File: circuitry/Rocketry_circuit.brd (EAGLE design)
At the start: 150 x 33 mm, 7 parts

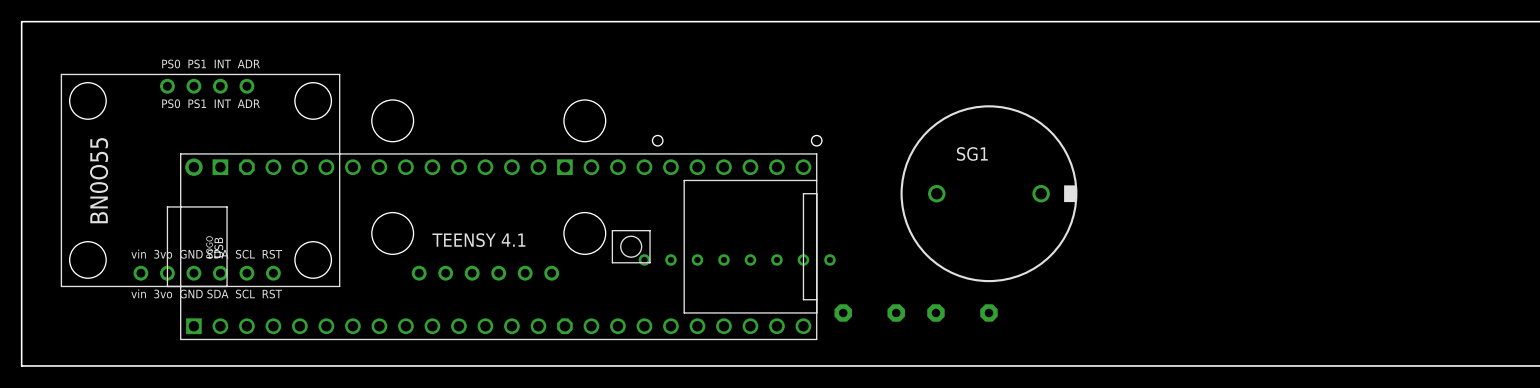
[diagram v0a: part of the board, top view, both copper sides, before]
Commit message: Added 3D files and proper footprints for all components, worked on brd design
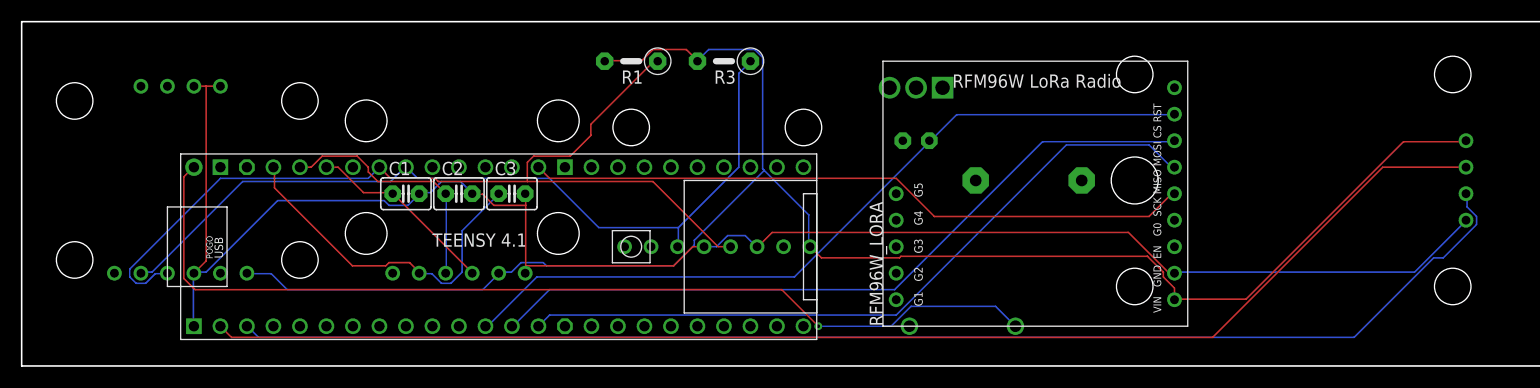
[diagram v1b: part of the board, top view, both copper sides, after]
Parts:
- removed SG1: EFBAA40D101, buzzer:EFBAA40D101
- added C1, C2, C3: 50p, capacitor-wima:C2.5-3
- added C4: 10u, capacitor-wima:C2.5-3
- added D1: 1N4004, diode:DO41-10
- added G1: 3V11R, battery:3V11R
- added IC1: TC1264-3.3VAB, TC1264-3.3VAB:TO254P483X988X2222-3P
- added U$4: NEO6M, NEO6M:NEO6M
- added U$5: RFM96W, RMF96W_lora:RFM96W
- moved R1 33.2 mm to (58.4, 29.2), flipped to the top
- moved R3 33.2 mm to (67.3, 29.2), flipped to the top
- moved BRKOUT1 27.9 mm to (2.54, 7.62), flipped to the bottom
- moved U$2 16.6 mm to (55.9, 8.89)
- moved U$3 2.54 mm to (30.5, 7.62)
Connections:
- new net N$1: C1.1, U$1.21-A7/RX5/BCLK1, U$3.X
- new net N$10: U$1.11-MOSI/CTX1, U$5.MOSI
- new net N$11: U$1.10-CS\MQSR, U$5.CS
- new net N$12: D1.A, G1.+, IC1.1
- new net N$2: C2.1, U$1.22-A8/CTX1, U$3.Y
- new net N$4: C3.1, U$1.23-A9/CRX1/MCLK1, U$3.Z
- new net N$6: U$1.0-RX1/CS1/CRX2, U$4.RX
- new net N$7: U$1.1-TX1/MISO1/CTX2, U$4.TX
- new net N$8: U$1.13-SCK/LED, U$5.SCK
- new net N$9: U$1.12-MISO/MQSL, U$5.MISO
- net +3V3: now also C4.1, IC1.3, U$2.VIN, U$3.3.3V, U$4.VCC, U$5.VIN
- net +5V: now also D1.C
- net GND: now also C1.2, C2.2, C3.2, C4.2, G1.-, IC1.2, U$2.GND, U$2.SDO, U$3.GND, U$4.GND, U$5.GND
- net N$3: now also U$1.19-A5/SCL0, U$2.SCK; no longer U$1.26-A12/MOSI1
- net N$5: now also U$1.18-A4/SDA0, U$2.SDI; no longer U$1.25-A11/RX6/SDA2
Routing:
- net GND: track 0.00 -> 166.8 mm
- net +3V3: track 0.00 -> 164.9 mm
- net N$6: track 0.00 -> 126.6 mm
- net N$7: track 0.00 -> 126.2 mm
- net +5V: track 0.00 -> 94.3 mm, vias 0 -> 1
- net N$3: track 0.00 -> 88.8 mm
- net N$5: track 0.00 -> 78.9 mm
- net N$11: track 0.00 -> 74.5 mm
- net N$10: track 0.00 -> 70.9 mm
- net N$9: track 0.00 -> 69.0 mm
- net N$8: track 0.00 -> 63.9 mm
- net N$4: track 0.00 -> 33.6 mm
- net N$2: track 0.00 -> 23.8 mm
- net N$1: track 0.00 -> 18.2 mm

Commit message: power circuitry up to date
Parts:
- added C5: 100u, capacitor-wima:C2.5-3
- added D2: 1N4004, diode:DO41-10
- moved G1 6.38 mm to (97.2, 24.1)
- moved IC1 6.38 mm to (81.9, 27.3), turned to 180 degrees
- moved D1 1.27 mm to (91.4, 3.81)
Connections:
- net +5V: now also D2.C
- net GND: now also C5.1
- net N$12: now also C5.2, D2.A
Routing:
- net GND: track 166.8 -> 0.00 mm
- net +3V3: track 164.9 -> 0.00 mm
- net N$6: track 126.6 -> 0.00 mm
- net N$7: track 126.2 -> 0.00 mm
- net +5V: track 94.3 -> 0.00 mm, vias 1 -> 0
- net N$3: track 88.8 -> 0.00 mm
- net N$5: track 78.9 -> 0.00 mm
- net N$11: track 74.5 -> 0.00 mm
- net N$10: track 70.9 -> 0.00 mm
- net N$9: track 69.0 -> 0.00 mm
- net N$8: track 63.9 -> 0.00 mm
- net N$4: track 33.6 -> 0.00 mm
- net N$2: track 23.8 -> 0.00 mm
- net N$1: track 18.2 -> 0.00 mm
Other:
- board text added: "Add Decals and names etc"
- board text added: "Add redundancy pads and connections"

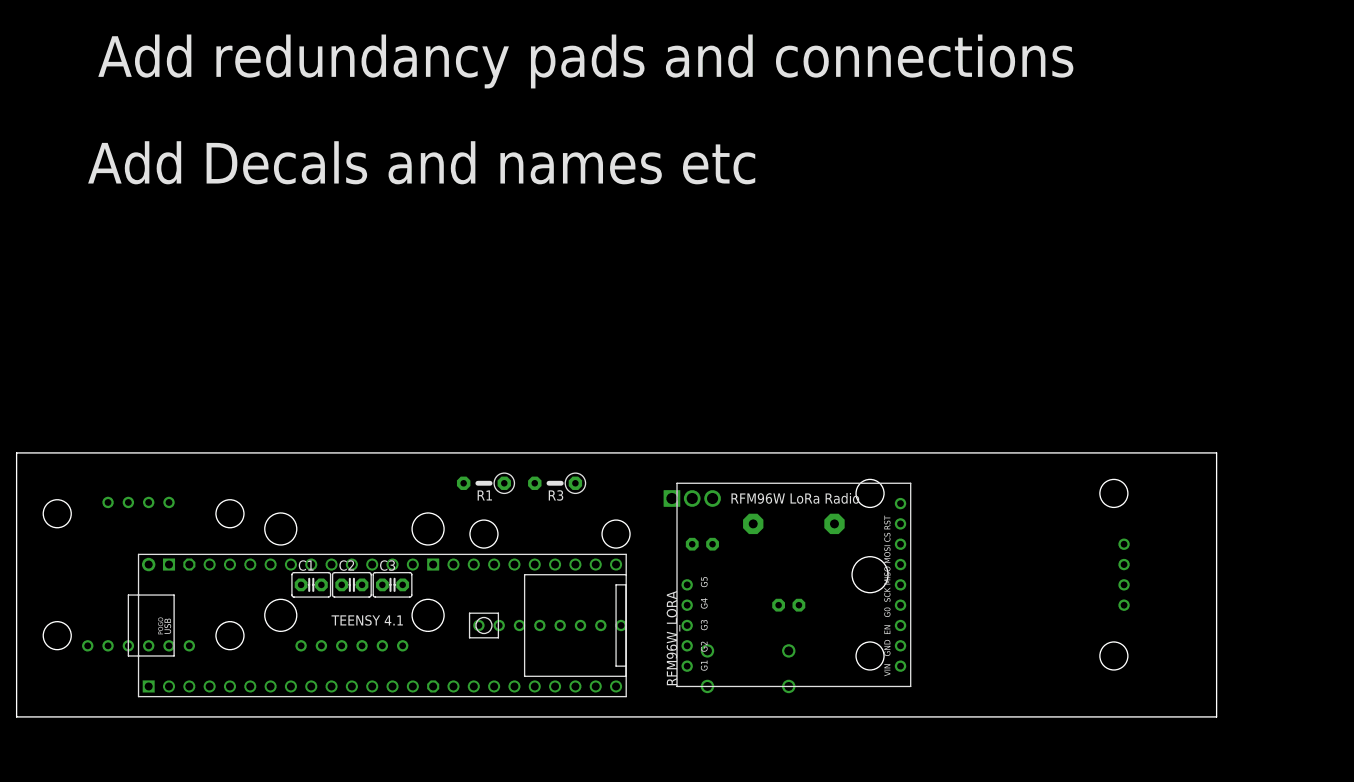
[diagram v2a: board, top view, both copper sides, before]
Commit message: updated board size to 31.75mm width, to fit into 34mm transition shoulder section
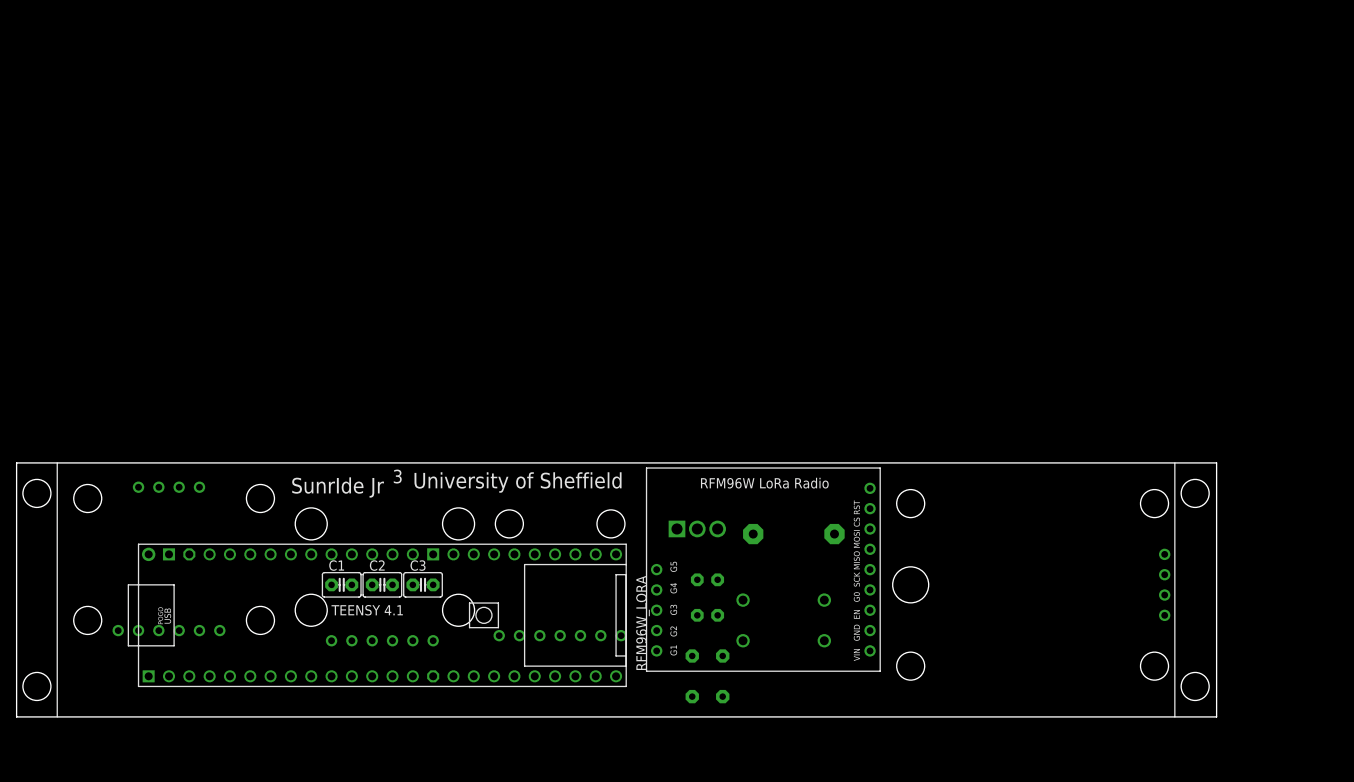
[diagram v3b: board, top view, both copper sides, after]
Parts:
- U$2: value BMP388 -> BMP280; device BMP388:BMP388 -> BMP280:BMP280
- moved R1 35.5 mm to (84.5, 5.08), flipped to the bottom, turned to 90 degrees
- moved R3 32.0 mm to (88.3, 5.08), flipped to the bottom, turned to 90 degrees
- moved C5 10.2 mm to (86.4, 12.7)
- moved D2 7.75 mm to (95.9, 14.6)
- moved D1 7.24 mm to (95.9, 9.53)
- moved U$4 5.24 mm to (144.8, 3.81)
- moved C4 4.49 mm to (86.4, 17.1)
- moved U$5 4.26 mm to (108.0, 5.71)
- moved BRKOUT1 4.26 mm to (6.35, 9.53)
- moved U$3 3.86 mm to (34.3, 8.26)
- moved IC1 3.86 mm to (82.5, 23.5)
- moved C1 3.81 mm to (40.6, 16.5)
- moved C2 3.81 mm to (45.7, 16.5)
- moved C3 3.81 mm to (50.8, 16.5)
- moved U$2 3.42 mm to (59.1, 7.62)
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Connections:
- net N$3: now also U$1.24-A10/TX6/SCL2
- net N$5: now also U$1.25-A11/RX6/SDA2
- net N$6: now also U$1.7-RX2/OUT1A
- net N$7: now also U$1.8-TX2/IN2
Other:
- board size 150 x 33 mm -> 150 x 31.8 mm
- board text added: ""In thrust we trust""
- board text added: "3"
- board text added: "SunrIde Jr"
- board text added: "University of Sheffield"
- board text removed: "Add Decals and names etc"
- board text removed: "Add redundancy pads and connections"

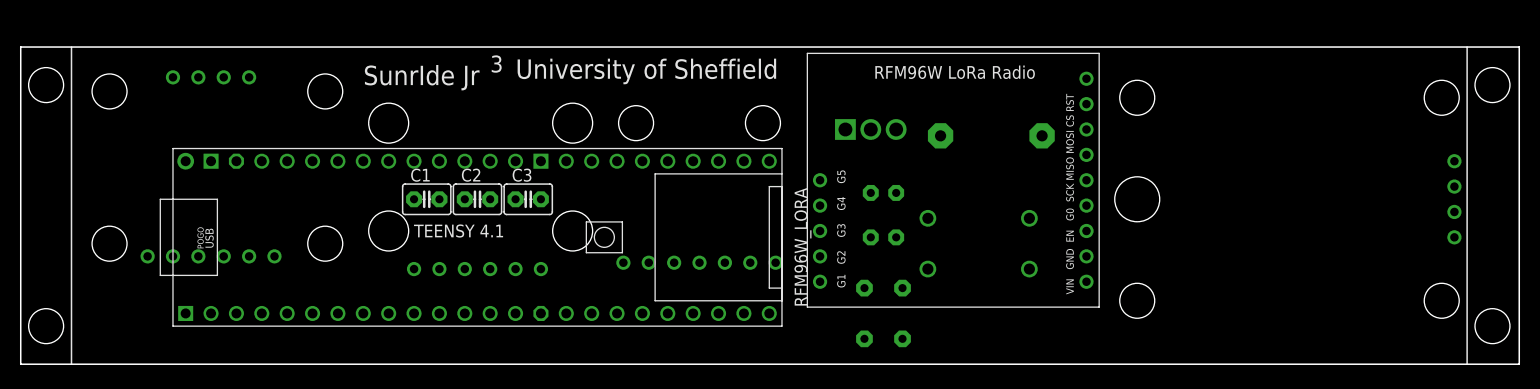
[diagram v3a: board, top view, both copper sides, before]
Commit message: Incremental progress - 5V for GPS, interrupt wire, etc
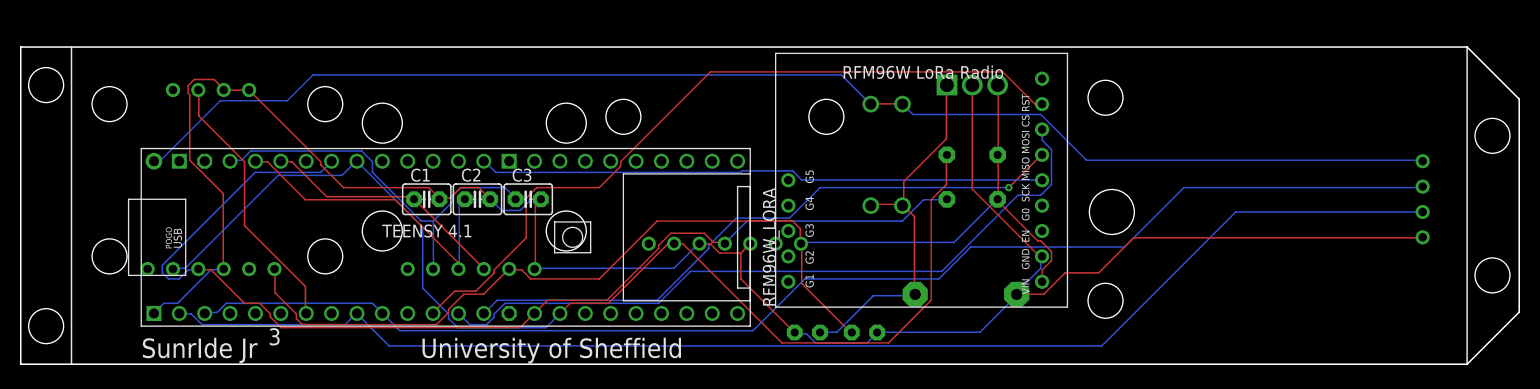
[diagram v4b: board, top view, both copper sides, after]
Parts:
- moved R3 17.3 mm to (95.2, 21.0), turned to 180 degrees
- moved G1 16.1 mm to (94.6, 6.99), turned to 180 degrees
- moved R1 15.7 mm to (95.2, 16.5), turned to 180 degrees
- moved D1 15.7 mm to (85.1, 21.0), turned to 270 degrees
- moved C4 14.1 mm to (84.5, 3.17), turned to 180 degrees
- moved C5 12.2 mm to (78.7, 3.17), turned to 180 degrees
- moved IC1 11.1 mm to (92.7, 27.9)
- moved D2 9.92 mm to (88.3, 21.0), turned to 270 degrees
- moved U$4 3.18 mm to (141.6, 3.81)
- moved U$1 3.18 mm to (43.8, 12.7)
- moved U$5 3.17 mm to (104.8, 5.71)
- moved U$2 2.29 mm to (57.8, 9.53)
- moved BRKOUT1 1.27 mm to (6.35, 8.26)
- moved U$3 0.63 mm to (33.7, 8.26)
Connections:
- new net N$13: BRKOUT1.INT, U$1.5-IN2
- net +3V3: no longer U$4.VCC
- net +5V: now also U$4.VCC
- net N$6: now also U$4.TX; no longer U$4.RX
- net N$7: now also U$4.RX; no longer U$4.TX
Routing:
- net GND: track 0.00 -> 205.1 mm
- net +5V: track 0.00 -> 134.2 mm
- net N$6: track 0.00 -> 132.3 mm
- net N$7: track 0.00 -> 129.5 mm
- net +3V3: track 0.00 -> 118.9 mm
- net N$5: track 0.00 -> 115.7 mm
- net N$3: track 0.00 -> 110.2 mm
- net N$11: track 0.00 -> 75.1 mm
- net N$10: track 0.00 -> 71.7 mm
- net N$9: track 0.00 -> 62.6 mm, vias 0 -> 1
- net N$8: track 0.00 -> 56.8 mm
- net N$4: track 0.00 -> 39.6 mm
- net N$12: track 0.00 -> 37.9 mm
- net N$2: track 0.00 -> 32.4 mm
- net N$13: track 0.00 -> 26.8 mm
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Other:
- outline, holes or cut-outs redrawn

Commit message: added a transisor and breakouts for spare teensy pins (incase we need them)
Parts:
- added G2, G3, G4: 3V11R, battery:3V11R
- added Q1: 2N3565, transistor-npn:TO92
- added U$6, U$7, U$8, U$9: 1PINOUT, 1PINOUT:1PINOUT
- C1, C2, C3: value 50p -> 50n
- moved G1 3.24 mm to (94.0, 10.2)
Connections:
- new net N$14: U$1.1-TX1/MISO1/CTX2, U$2.SDO
- new net N$15: U$1.27-A13/SCK1, U$2.SCK
- new net N$16: U$1.0-RX1/CS1/CRX2, U$2.CS
- new net N$17: U$1.26-A12/MOSI1, U$2.SDI
- new net N$18: U$1.2-OUT2, U$5.G0
- new net N$19: U$1.3-LRCLK2, U$5.G1
- new net N$20: U$1.9-OUT1C, U$5.RST
- new net N$21: U$1.36-PWM, U$5.G4
- new net N$22: U$1.37-PWM, U$5.G5
- new net N$23: Q1.2, U$1.32-OUT1B
- new net N$24: Q1.1, U$4.GND
- new net N$25: U$1.31-CTX3, U$6.PIN1
- new net N$26: U$1.41-A17/MISO1, U$7.PIN1
- new net N$27: U$1.30-CRX3, U$8.PIN1
- new net N$28: U$1.40-A16/CS1, U$9.PIN1
- net GND: now also G2.-, G3.-, G4.-, Q1.3; no longer U$2.SDO, U$4.GND
- net N$12: now also G2.+, G3.+, G4.+
- net N$3: no longer U$2.SCK
- net N$5: no longer U$2.SDI
- net N$6: now also U$1.28-RX7; no longer U$1.0-RX1/CS1/CRX2
- net N$7: now also U$1.29-TX7; no longer U$1.1-TX1/MISO1/CTX2
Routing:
- net GND: track 205.1 -> 0.00 mm
- net +5V: track 134.2 -> 0.00 mm
- net N$6: track 132.3 -> 0.00 mm
- net N$7: track 129.5 -> 0.00 mm
- net +3V3: track 118.9 -> 0.00 mm
- net N$5: track 115.7 -> 0.00 mm
- net N$3: track 110.2 -> 0.00 mm
- net N$11: track 75.1 -> 0.00 mm
- net N$10: track 71.7 -> 0.00 mm
- net N$9: track 62.6 -> 0.00 mm, vias 1 -> 0
- net N$8: track 56.8 -> 0.00 mm
- net N$4: track 39.6 -> 0.00 mm
- net N$12: track 37.9 -> 0.00 mm
- net N$2: track 32.4 -> 0.00 mm
- net N$13: track 26.8 -> 0.00 mm
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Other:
- board text removed: ""In thrust we trust""

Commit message: Final sch and brd files - Ordered pcb
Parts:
- removed G2, G3: 3V11R, battery:3V11R
- added U$10, U$11, U$13, U$14, U$15, U$16: 1PINOUT, 1PINOUT:1PINOUT
- added U$12: SMALL_SCREW_TERMINAL, SMALL_SCREW_TERMINAL:SMALL_SCREW_TERMINAL
- moved U$6 66.0 mm to (8.89, 2.54)
- moved U$8 61.0 mm to (11.4, 2.54)
- moved G1 33.9 mm to (127.0, 2.54), flipped to the top
- moved U$7 21.6 mm to (58.4, 2.54)
- moved U$9 21.6 mm to (55.9, 2.54)
- moved G4 14.0 mm to (96.5, 3.81), turned to 180 degrees
- moved Q1 1.27 mm to (87.6, 11.4)
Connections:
- removed net N$14 (its old number): U$1.1-TX1/MISO1/CTX2, U$2.SDO
- removed net N$28: U$1.40-A16/CS1, U$9.PIN1
- new net N$18: U$1.28-RX7, U$6.PIN1
- net GND: now also U$10.PIN1, U$11.PIN1, U$12.GND, U$3.ST; no longer G2.-, G3.-
- net N$10: now also U$2.SDI
- net N$11: now also U$1.37-PWM; no longer U$1.10-CS\MQSR
- net N$12: now also U$12.V+; no longer G2.+, G3.+
- net N$15: now also U$1.24-A10/TX6/SCL2, U$9.PIN1; no longer U$1.27-A13/SCK1, U$2.SCK
- net N$16: now also U$1.10-CS\MQSR; no longer U$1.0-RX1/CS1/CRX2
- net N$17: now also U$1.25-A11/RX6/SDA2, U$7.PIN1; no longer U$1.26-A12/MOSI1, U$2.SDI
- net N$21: now also U$1.29-TX7, U$8.PIN1; no longer U$1.36-PWM, U$5.G4
- net N$22: now also U$1.26-A12/MOSI1, U$13.PIN1; no longer U$1.37-PWM, U$5.G5
- net N$25: now also U$1.27-A13/SCK1, U$14.PIN1; no longer U$1.31-CTX3, U$6.PIN1
- net N$26: now also U$1.0-RX1/CS1/CRX2, U$15.PIN1; no longer U$1.41-A17/MISO1, U$7.PIN1
- net N$27: now also U$1.1-TX1/MISO1/CTX2, U$16.PIN1; no longer U$1.30-CRX3, U$8.PIN1
- net N$3: now also U$1.18-A4/SDA0; no longer U$1.19-A5/SCL0, U$1.24-A10/TX6/SCL2
- net N$5: now also U$1.19-A5/SCL0; no longer U$1.18-A4/SDA0, U$1.25-A11/RX6/SDA2
- net N$6: no longer U$1.28-RX7
- net N$7: no longer U$1.29-TX7
- net N$8: now also U$2.SCK
- net N$9: now also U$2.SDO
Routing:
- net GND: track 0.00 -> 237.6 mm
- net +5V: track 0.00 -> 135.8 mm
- net N$20: track 0.00 -> 131.8 mm, vias 0 -> 1
- net N$6: track 0.00 -> 114.4 mm
- net N$7: track 0.00 -> 113.2 mm
- net +3V3: track 0.00 -> 111.0 mm
- net N$3: track 0.00 -> 106.5 mm, vias 0 -> 3
- net N$12: track 0.00 -> 96.5 mm, vias 0 -> 1
- net N$14: track 0.00 -> 89.0 mm, vias 0 -> 1
- net N$5: track 0.00 -> 87.9 mm
- net N$10: track 0.00 -> 85.9 mm, vias 0 -> 3
- net N$8: track 0.00 -> 82.5 mm, vias 0 -> 1
- net N$18: track 0.00 -> 81.7 mm, vias 0 -> 1
- net N$9: track 0.00 -> 65.2 mm, vias 0 -> 2
- net N$19: track 0.00 -> 58.5 mm, vias 0 -> 1
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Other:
- board text added: ""In thrust we trust""
- board text added: "Daedalus"
- board text removed: "3"
- board text removed: "SunrIde Jr"
